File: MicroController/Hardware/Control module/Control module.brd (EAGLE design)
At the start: 100 x 70 mm, 110 parts, among them J2 0446200002, J3 0446200002, J4 0446200002, Q1 BSS138, Q10 BSS138, Q11 BSS138, Q12 BSS138, Q2 BSS138, Q3 BSS138, Q4 BSS138, Q5 BSS138, Q6 BSS138, Q7 BSS138, Q8 BSS138, Q9 BSS138, U1 XMEGA-A3-AU, U2 7812DT, U3 TLV1117-33CDCY, U4 CD4051BM, U5 TB6621FNG, U6 TXB0108PWR, U7 TXB0108PWR, U8 LM2937IMP-5.0, U9 CD74HC4067SM96

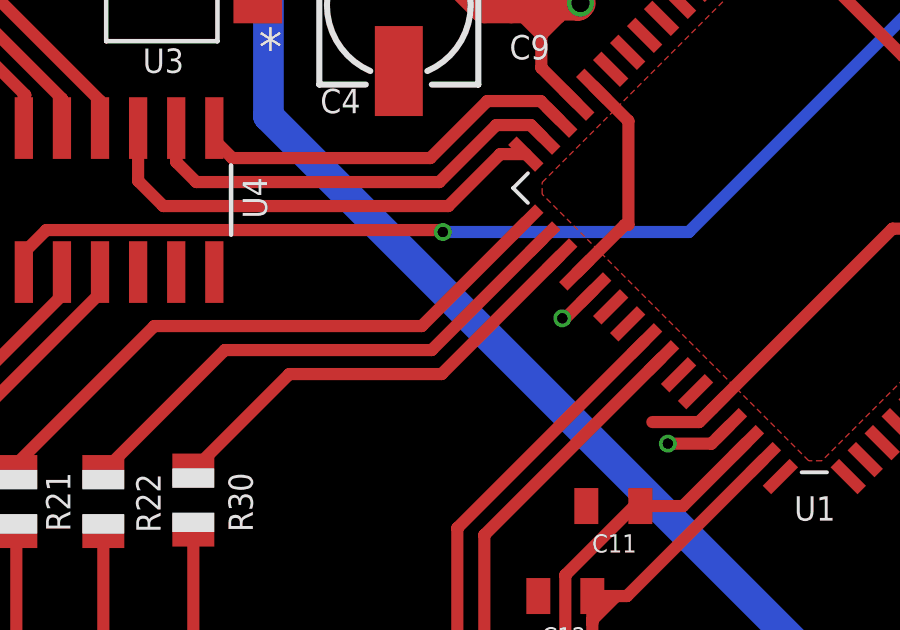
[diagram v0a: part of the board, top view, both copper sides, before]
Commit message: Moved the LED connection to another pin.
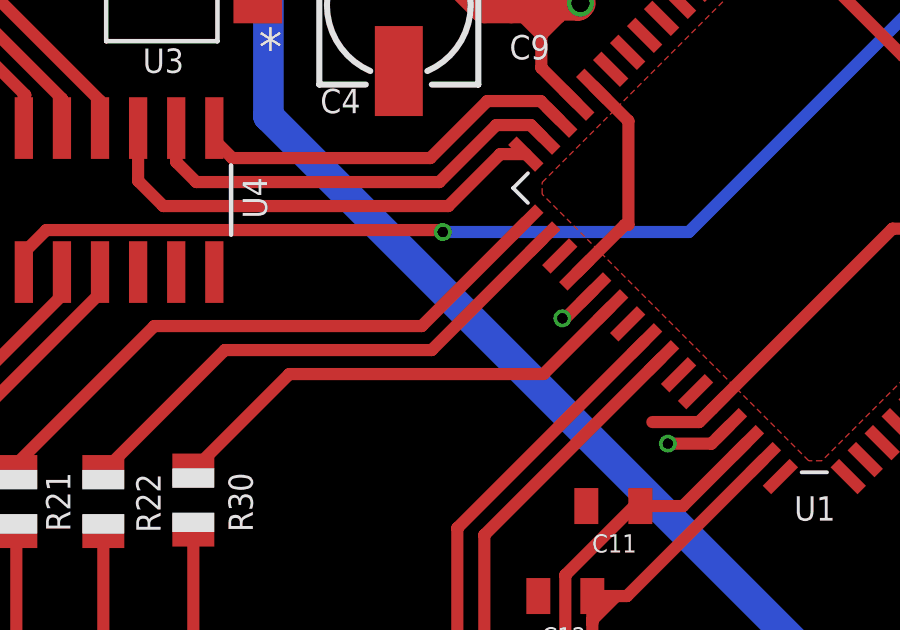
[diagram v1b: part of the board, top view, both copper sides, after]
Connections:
- net LED_3: now also U1.54; no longer U1.51
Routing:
- net LED_3: track 15.2 -> 16.2 mm
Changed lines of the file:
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@@
 </signal>
 <signal name="LED_3">
-<contactref element="U1" pad="51"/>
 <contactref element="R30" pad="2"/>
 <wire x1="24.3" y1="30.6" x2="27.5" y2="33.8" width="0.4064" layer="1"/>
-<wire x1="32.577459375" y1="33.8" x2="36.514715625" y2="37.73725625" width="0.4064" layer="1"/>
-<wire x1="27.5" y1="33.8" x2="32.577459375" y2="33.8" width="0.4064" layer="1"/>
+<contactref element="U1" pad="54"/>
+<wire x1="35.971571875" y1="33.8" x2="38.211771875" y2="36.0402" width="0.4064" layer="1"/>
+<wire x1="27.5" y1="33.8" x2="35.971571875" y2="33.8" width="0.4064" layer="1"/>
 </signal>
 <signal name="N$4">

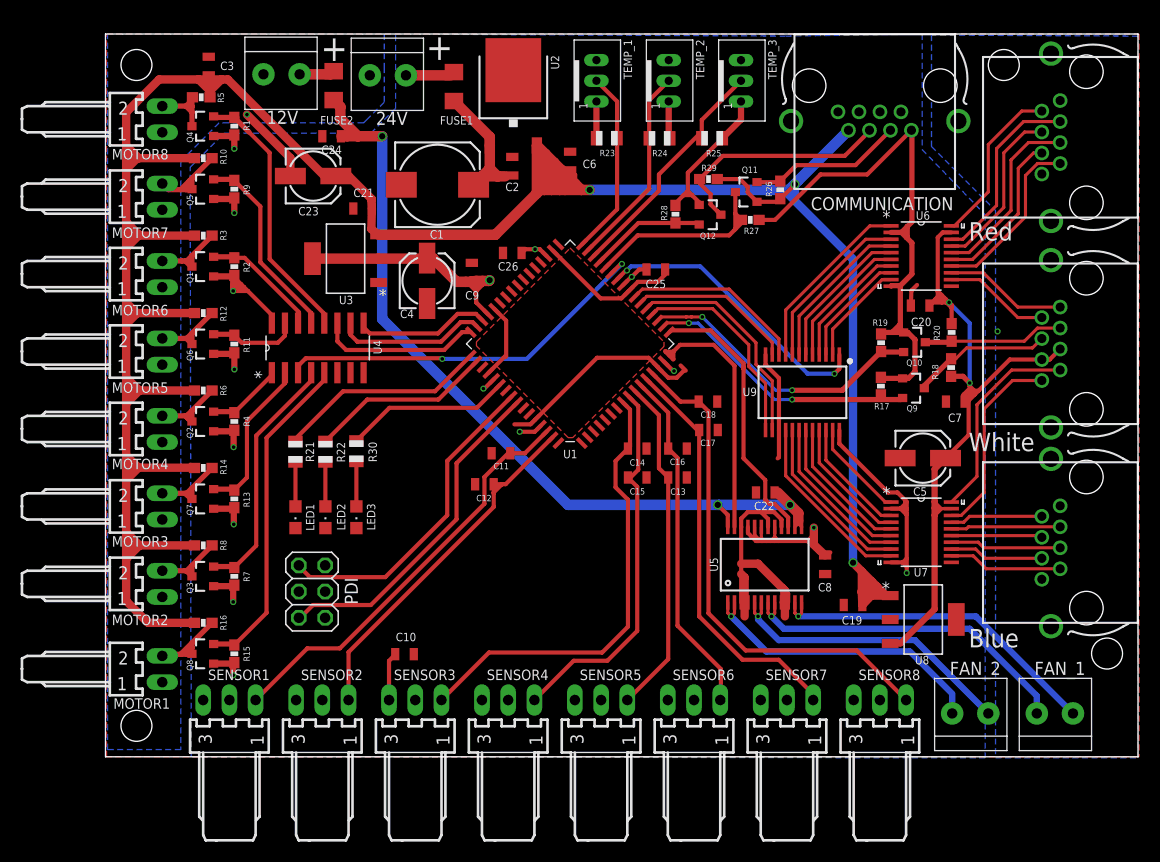
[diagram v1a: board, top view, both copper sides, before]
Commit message: Many changes in this new version of the Control PCB.
The motor drivers are replaced by MOSFET's.
The schematic is much better organized. 
Small additional changes.
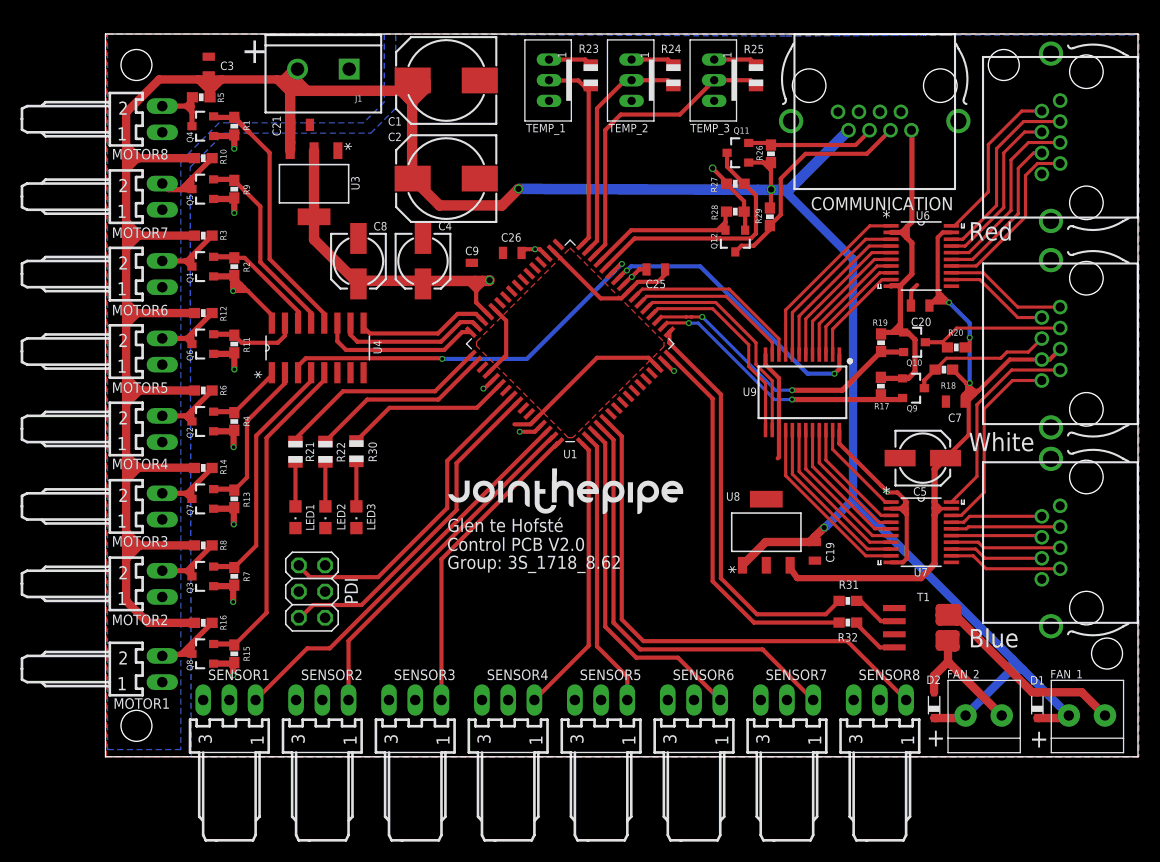
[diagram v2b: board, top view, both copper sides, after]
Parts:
- removed 12V, 24V: 1X2-3.5MM, adafruit:1X2-3.5MM
- removed C10, C11, C12, C13, C14, C15, C16, C17, C18, C22, C24, C6: 1.0uF, SparkFun-Capacitors:0805
- removed C23: 22uF, adafruit:153CLV-0505
- removed FUSE1, FUSE2: 6V/0.5A, SparkFun-Fuses:1206
- removed U2: 7812DT, adafruit:TO252
- removed U5: TB6621FNG, SparkFun:SSOP24
- added D1, D2: BAT60J, diode:SOD323_ST
- added J1: (no value), SparkFun-Connectors:SCREWTERMINAL-5MM-2
- added R31, R32: 1K, SparkFun:0603-RES
- added T1: SI4804CDY-T1-GE3, zetex:SO8
- C1: value 220uF -> (none); device adafruit:175TMP-0810 -> adafruit:150CLZ-0810
- C2: value 1.0uF -> (none); device SparkFun-Capacitors:0805 -> adafruit:150CLZ-0810
- C8: value 1.0uF -> 22uF; device SparkFun-Capacitors:0805 -> adafruit:153CLV-0505
- moved C8 53.9 mm to (24.5, 48.0)
- moved U8 17.4 mm to (64.0, 21.8), turned to 90 degrees
- moved C1 10.1 mm to (33.0, 65.5), turned to 180 degrees
- moved C21 10.1 mm to (18.9, 61.2), turned to 0 degrees
- moved U3 7.87 mm to (20.2, 55.5), turned to 270 degrees
- moved R25 7.43 mm to (63.0, 66.0), turned to 270 degrees
- moved R29 6.98 mm to (64.3, 52.3), turned to 270 degrees
- moved C2 6.51 mm to (33.0, 56.0), turned to 180 degrees
- moved C19 6.38 mm to (68.7, 19.9), turned to 270 degrees
- moved R23 6.28 mm to (47.0, 66.0), turned to 270 degrees
- moved R24 6.24 mm to (55.0, 66.0), turned to 270 degrees
- moved R28 5.81 mm to (61.0, 52.8), turned to 180 degrees
- moved TEMP_1 4.50 mm to (43.0, 65.5), turned to 90 degrees
- moved Q11 3.88 mm to (61.3, 58.5)
- moved R27 3.79 mm to (61.0, 55.5), turned to 0 degrees
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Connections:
- removed net +24V: C1.+, C2.1, FUSE1.2, U2.1
- removed net 12V_FANS: C22.1, C24.1, FUSE2.2, U5.13, U5.14, U5.24
- removed net FAN_1+: FAN_1.1, U5.11, U5.12
- removed net FAN_1-: FAN_1.2, U5.7, U5.8
- removed net FAN_1_CONTROL: U1.16, U5.23
- removed net FAN_2+: FAN_2.2, U5.1, U5.2
- removed net FAN_2-: FAN_2.1, U5.5, U5.6
- removed net FAN_2_CONTROL: U1.17, U5.15
- removed net RX_RASPI: COMMUNICATION.4, Q12.3, R29.2
- removed net TX_RASPI: COMMUNICATION.6, Q11.2, R26.2
- removed net VIN: 24V.2, FUSE1.1
- new net FAN_ROW_1_PWM: R31.1, U1.17
- new net FAN_ROW_2_PWM: R32.1, U1.16
- new net N$2: R31.2, T1.2
- new net N$5: D2.A, FAN_2.1, T1.5, T1.6
- new net N$6: R32.2, T1.4
- new net RX: Q11.3, R27.2, U1.28
- new net TX: Q12.2, R28.2, U1.29
- net +12V: now also C1.+, C2.+, D1.C, D2.C, FAN_1.2, FAN_2.2, J1.2; no longer C23.+, C6.1, U2.2
- net GND: now also C2.-, C8.-, J1.1, T1.1, T1.3; no longer 12V.1, 24V.1, C10.2, C11.2, C12.2, C13.2, C14.2, C15.2, C16.2, C17.2, C18.2, C2.2, C22.2, C23.-, C24.2, C6.2, C8.2, U2.3, U5.10, U5.16, U5.18, U5.22, U5.3, U5.4, U5.9
- net IR_1: no longer C11.1
- net IR_2: no longer C12.1
- net IR_3: now also U1.64; no longer C14.1, U1.8
- net IR_4: now also U1.1; no longer C15.1, U1.9
- net IR_5: now also U1.2; no longer C13.1, U1.10
- net IR_6: now also U1.3; no longer C16.1, U1.11
- net IR_7: now also U1.4; no longer C17.1, U1.12
- net IR_8: now also U1.5; no longer C18.1, U1.13
- net N$7: now also D1.A, FAN_1.1, T1.7, T1.8; no longer 12V.2, FUSE2.1
- net RX_ATXMEGA: now also COMMUNICATION.4, Q11.2, R26.2; no longer Q11.3, R27.2, U1.28
- net TX_ATXMEGA: now also COMMUNICATION.6, Q12.3, R29.2; no longer Q12.2, R28.2, U1.29
- net VCC: now also C8.+; no longer C10.1, C8.1, U5.17, U5.19, U5.20, U5.21
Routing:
- net 12V_FANS: track 81.4 -> 0.00 mm, vias 3 -> 0
- net GND: track 93.4 -> 51.6 mm, vias 2 -> 0
- net FAN_ROW_1_PWM: track 0.00 -> 39.6 mm
- net FAN_ROW_2_PWM: track 0.00 -> 37.5 mm
- net VCC: track 199.4 -> 162.5 mm
- net +12V: track 291.9 -> 326.6 mm
- net FAN_1-: track 33.6 -> 0.00 mm, vias 1 -> 0
- net FAN_1+: track 33.5 -> 0.00 mm, vias 1 -> 0
- net FAN_2+: track 29.4 -> 0.00 mm, vias 1 -> 0
- net FAN_2-: track 29.3 -> 0.00 mm, vias 1 -> 0
- net FAN_2_CONTROL: track 26.5 -> 0.00 mm
- net FAN_1_CONTROL: track 25.7 -> 0.00 mm
- net RX: track 0.00 -> 25.0 mm
- net N$7: track 3.42 -> 27.9 mm
- net RX_RASPI: track 23.2 -> 0.00 mm
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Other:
- board text added: "Control PCB V2.0"
- board text added: "Glen te Hofsté"
- board text added: "Group: 3S_1718_8.62"

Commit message: Finished the Control PCB version 2.0
Not a lot of changes where made comparing to the previous version of the PCB. Most noticeably the way the fans are controlled has changed. Further some small things that where found out during tests with the previous version.
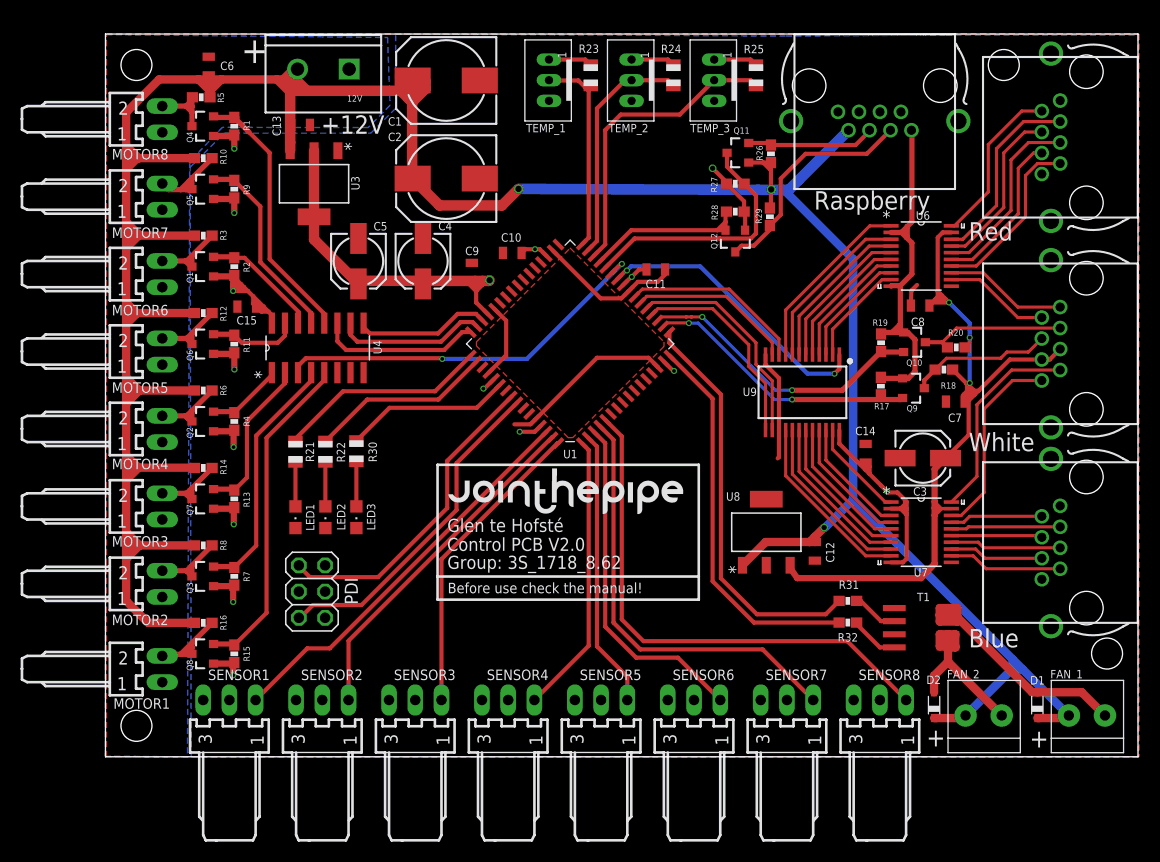
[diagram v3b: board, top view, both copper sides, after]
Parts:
- removed C20: 1.0uF, SparkFun-Capacitors:0805
- added C14, C15, C6: 100nF, SparkFun-Capacitors:0805
- C1, C2: value (none) -> 100uF
- C10, C11, C12, C13, C7, C9: value 1.0uF -> 100nF
- C3: value 1.0uF -> 22uF; device SparkFun-Capacitors:0805 -> adafruit:153CLV-0505
- C8: value 22uF -> 100nF; device adafruit:153CLV-0505 -> SparkFun-Capacitors:0805
- moved C3 78.9 mm to (79.2, 28.9), turned to 0 degrees
- moved C5 57.9 mm to (24.5, 48.0), turned to 270 degrees
- moved C8 54.6 mm to (78.9, 43.7), turned to 180 degrees
- renumbered C19 to C12, C21 to C13, C25 to C11, C26 to C10, COMMUNICATION to RJ45_COMM, J1 to 12V, J2 to RJ45_WHITE, J3 to RJ45_BLUE, J4 to RJ45_RED
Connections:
- net +12V: now also C6.1; no longer C3.1
- net +5V: now also C3.+, C8.1; no longer C20.1, C5.+
- net GND: now also C14.2, C15.2, C3.-, C6.2, C8.2; no longer C20.2, C3.2, C8.-
- net VCC: now also C14.1, C15.1, C5.+; no longer C8.+
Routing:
- net VCC: track 162.5 -> 168.1 mm
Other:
- board text added: "+12V"
- board text added: "Before use check the manual!"
- board text added: "Raspberry"
